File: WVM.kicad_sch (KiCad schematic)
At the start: 35 parts, among them J1 USB4215-03-A_REVA, P1 S2B-PH-SM4-TB, Q1 BSS138, Q2 BSS138, SW1 SW_SPST, SW2 SW_SPST, U1 NORA-W106-00B, U2 CH340C, U3 IIS3DWBTR, U4 TPS63036YFGT, U5 TP4056-42-ESOP8, U6 MCP9808_DFN

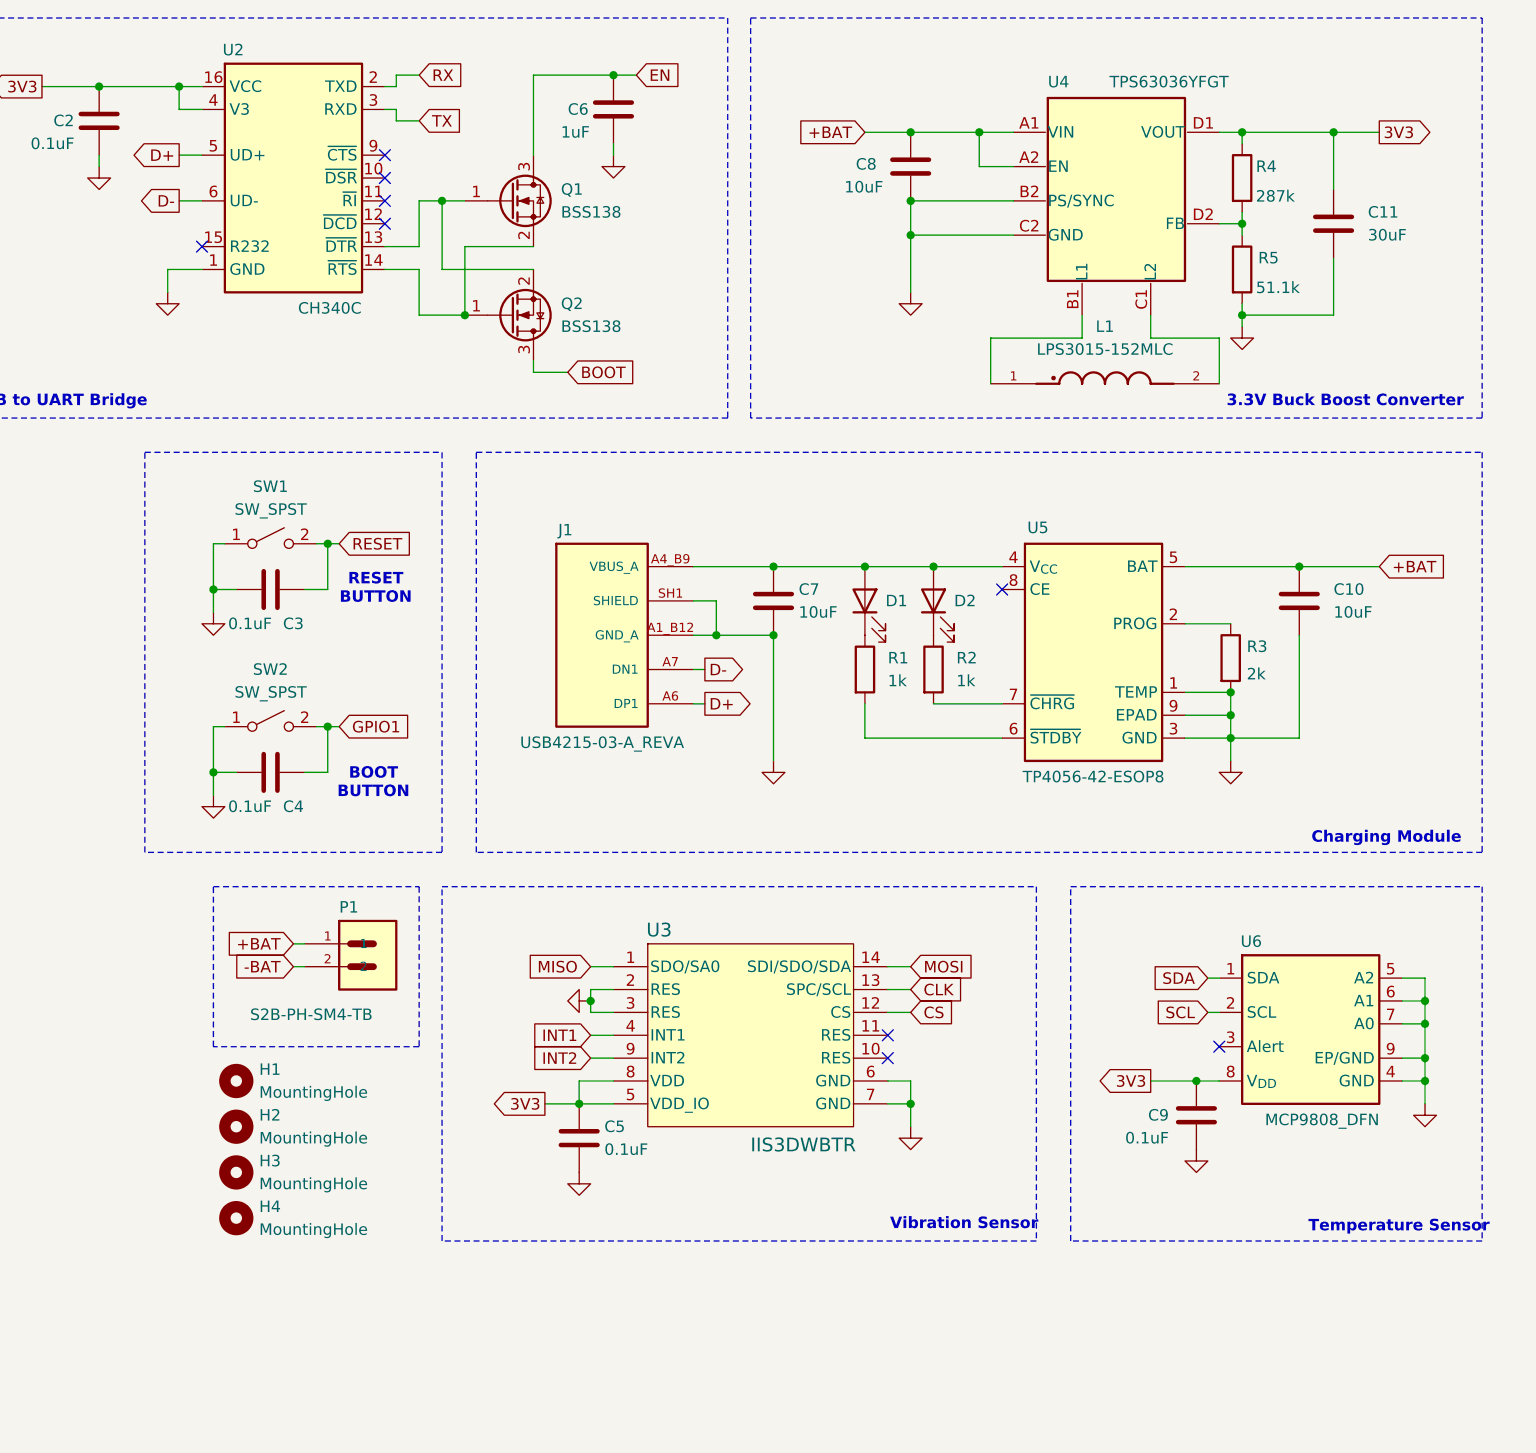
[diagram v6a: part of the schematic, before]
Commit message: Part Placement completed with board outline
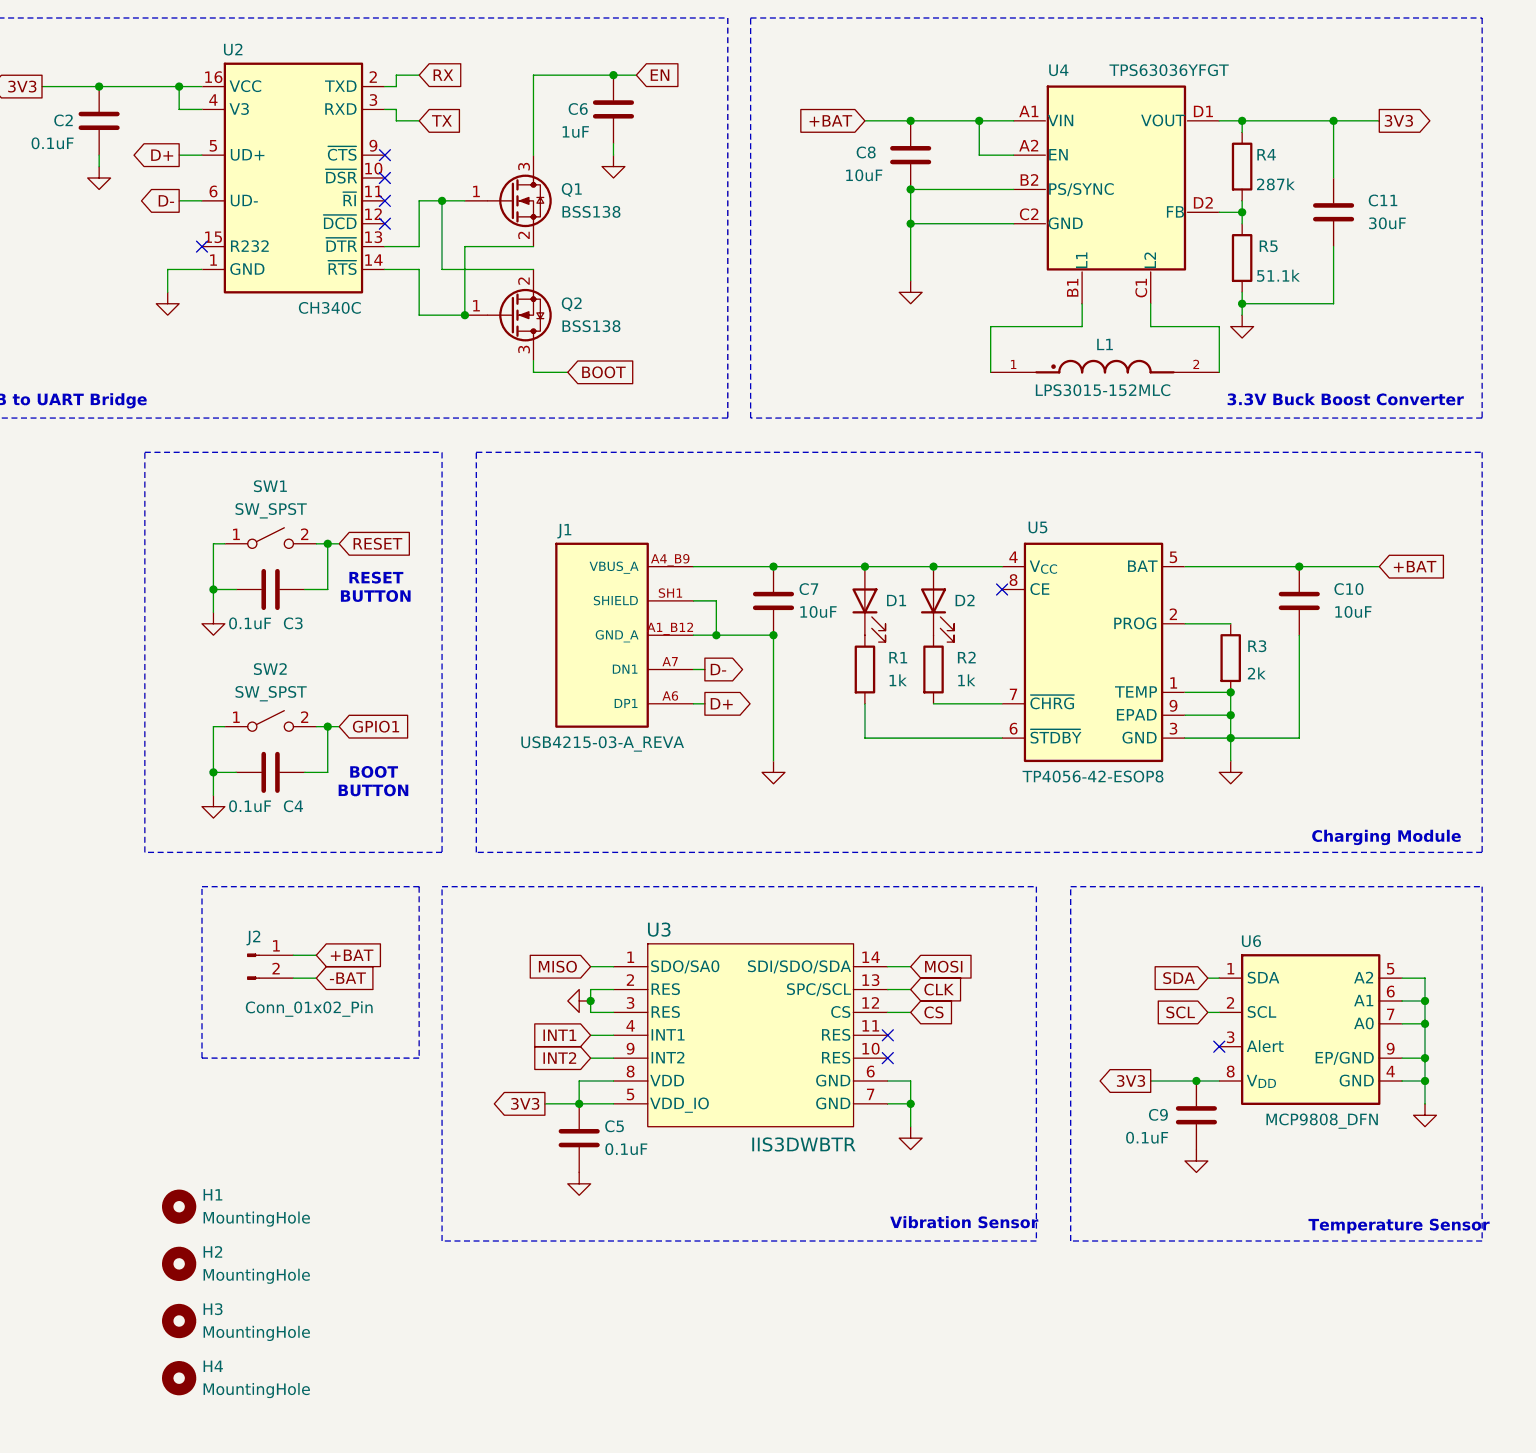
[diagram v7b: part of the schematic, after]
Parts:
- removed P1: S2B-PH-SM4-TB, S2B_PH_SM4_TB:JST_S2B-PH-SM4-TB, symbol S2B-PH-SM4-TB:S2B-PH-SM4-TB
- added J2: Conn_01x02_Pin, symbol Connector:Conn_01x02_Pin
- H1, H2, H3, H4: footprint MountingHole:MountingHole_2.2mm_M2 -> MountingHole:MountingHole_2.2mm_M2_Pad_Via
- L1: footprint LPS3015-152MLC:IND_LPS3015-152MLC -> LP3051:IND_LPS3015-152MLC
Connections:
- net +BAT: now also J2.1 (Pin_1)
- net -BAT: now also J2.2 (Pin_2)
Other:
- moved on the sheet: C11, C8, H1, H2, H3, H4, R4, R5, U4

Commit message: saved commit 13.10.25
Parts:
- J2: footprint (none) -> Bat_pad:Untitled
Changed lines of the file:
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@@
 			)
 		)
-		(property "Footprint" ""
+		(property "Footprint" "Bat_pad:Untitled"
 			(at 140.97 124.46 0)
 			(effects
